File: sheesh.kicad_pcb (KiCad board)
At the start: 2 copper layers, 234.7 x 104.6 mm, 104 parts, among them J1 3305-0-15-80-47-27-10-0, J10 3305-0-15-80-47-27-10-0, J11 3305-0-15-80-47-27-10-0, J12 3305-0-15-80-47-27-10-0, J13 3305-0-15-80-47-27-10-0, J14 3305-0-15-80-47-27-10-0, J15 3305-0-15-80-47-27-10-0, J16 3305-0-15-80-47-27-10-0, J17 3305-0-15-80-47-27-10-0, J18 3305-0-15-80-47-27-10-0, J19 3305-0-15-80-47-27-10-0, J2 3305-0-15-80-47-27-10-0, J20 3305-0-15-80-47-27-10-0, J21 3305-0-15-80-47-27-10-0, J22 3305-0-15-80-47-27-10-0, J23 3305-0-15-80-47-27-10-0, J24 3305-0-15-80-47-27-10-0, J25 3305-0-15-80-47-27-10-0, J26 3305-0-15-80-47-27-10-0, J27 3305-0-15-80-47-27-10-0, J28 3305-0-15-80-47-27-10-0, J29 3305-0-15-80-47-27-10-0, J3 3305-0-15-80-47-27-10-0, J30 3305-0-15-80-47-27-10-0, J31 3305-0-15-80-47-27-10-0, J32 3305-0-15-80-47-27-10-0, J33 3305-0-15-80-47-27-10-0, J34 3305-0-15-80-47-27-10-0, J35 3305-0-15-80-47-27-10-0, J36 3305-0-15-80-47-27-10-0, J37 3305-0-15-80-47-27-10-0, J38 3305-0-15-80-47-27-10-0, J39 3305-0-15-80-47-27-10-0, J4 3305-0-15-80-47-27-10-0, J40 3305-0-15-80-47-27-10-0, J41 3305-0-15-80-47-27-10-0, J42 3305-0-15-80-47-27-10-0, J43 3305-0-15-80-47-27-10-0, J44 3305-0-15-80-47-27-10-0, J45 3305-0-15-80-47-27-10-0, J46 3305-0-15-80-47-27-10-0, J47 3305-0-15-80-47-27-10-0, J48 3305-0-15-80-47-27-10-0, J49 3305-0-15-80-47-27-10-0, J5 3305-0-15-80-47-27-10-0, J50 3305-0-15-80-47-27-10-0, J51 3305-0-15-80-47-27-10-0, J52 3305-0-15-80-47-27-10-0, J53 3305-0-15-80-47-27-10-0, J54 3305-0-15-80-47-27-10-0, J55 3305-0-15-80-47-27-10-0, J56 3305-0-15-80-47-27-10-0, J57 310-13-107-41-001000, J58 310-13-107-41-001000, J59 YZ00615050R-04, J6 3305-0-15-80-47-27-10-0, J60 YZ00615050R-04, J61 YZ00615050R-04, J62 YZ00615050R-04, J63 YZ00615050R-04, J64 310-13-107-41-001000, J65 310-13-107-41-001000, J66 YZ00615050R-04, J67 YZ00615050R-04, J68 YZ00615050R-04, J69 YZ00615050R-04, J7 3305-0-15-80-47-27-10-0, J70 YZ00615050R-04, J8 3305-0-15-80-47-27-10-0, J9 3305-0-15-80-47-27-10-0, SW1 SW_Push, SW10 SW_Push, SW11 SW_Push, SW12 SW_Push, SW13 SW_Push, SW14 SW_Push, SW15 SW_Push, SW16 SW_Push, SW17 SW_Push, SW18 SW_Push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

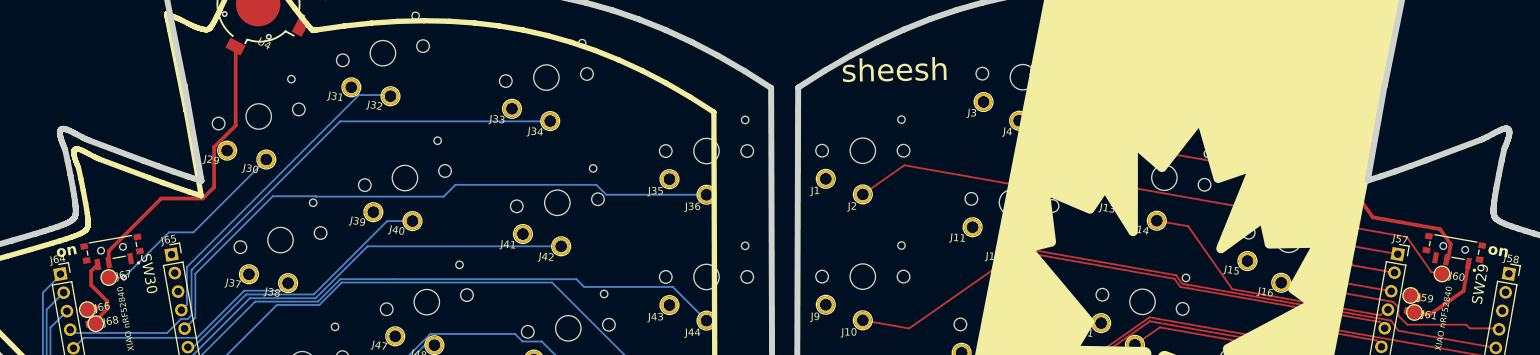
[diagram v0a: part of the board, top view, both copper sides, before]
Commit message: fix(sw-th_ssss811101): swap SW29 & SW30 symbol & footprint
Change PCM12SMTR to SSSS811101. The latter fits on the former's footprint, but the location was
slightly off fin  the cpl
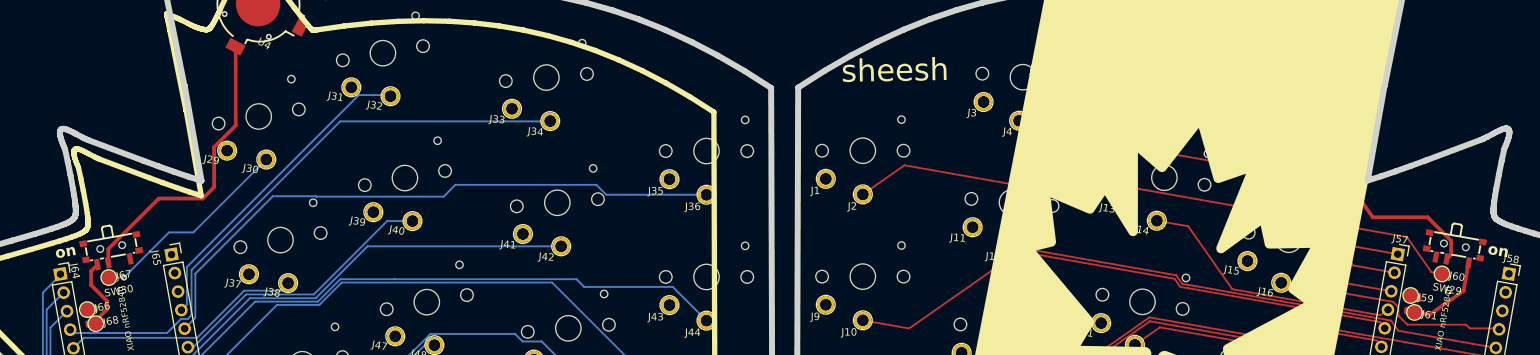
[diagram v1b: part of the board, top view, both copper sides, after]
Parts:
- SW29, SW30: footprint Sheesh:SW_PCM12SMTR -> Sheesh:SW-SMD_SSSS811101
- moved SW30 0.22 mm to (68.3, 90.8)
- moved SW29 0.10 mm to (249.6, 90.6)
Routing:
- net Net-(SW29-Pad2): track 39.7 -> 40.3 mm

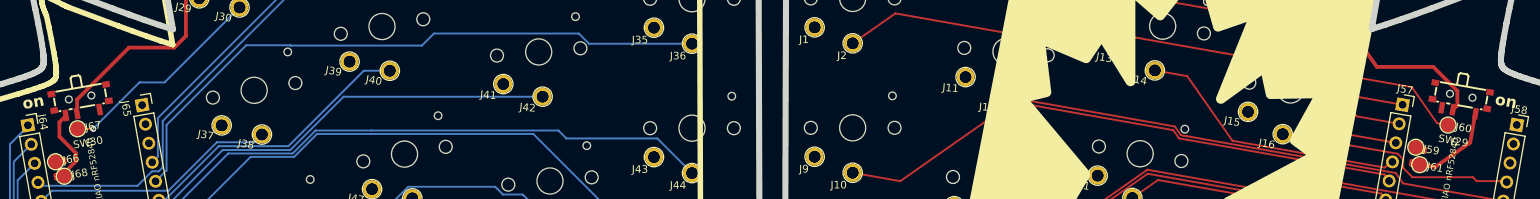
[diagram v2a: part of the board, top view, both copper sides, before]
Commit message: style(component): nudge switch away from pogo pin
nudge power switch for more comfortable clearance
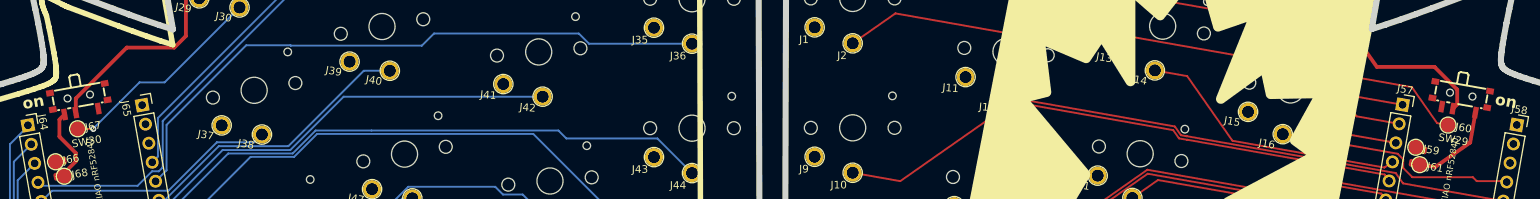
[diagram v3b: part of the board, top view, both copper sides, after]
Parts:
- moved SW30 0.22 mm to (68.2, 90.7)
- moved SW29 0.15 mm to (249.6, 90.4)
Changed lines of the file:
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@@
 		(fp_line
 			(start -8.63 -8.5)
-			(end 8.599913 -8.5)
+			(end 8.599912 -8.5)
 			(stroke
 				(width 0.12)
@@
 		(fp_arc
 			(start -8.994012 -8.099594)
-			(mid -8.898744 -8.378652)
+			(mid -8.898744 -8.378651)
 			(end -8.63 -8.5)
 			(stroke
@@
 		)
 		(fp_arc
-			(start 8.599913 -8.5)
-			(mid 8.878978 -8.404734)
+			(start 8.599912 -8.5)
+			(mid 8.878977 -8.404735)
 			(end 9.000321 -8.135989)
 			(stroke
@@
 		(fp_poly
 			(pts
-				(xy -1.1 -1.100002) (xy 1.100002 -1.1) (xy 1.1 1.100002) (xy -1.100002 1.1)
+				(xy -1.1 -1.100003) (xy 1.100003 -1.1) (xy 1.1 1.100003) (xy -1.100003 1.1)
 			)
 			(stroke
@@
 		(fp_line
 			(start -8.63 -8.5)
-			(end 8.599913 -8.5)
+			(end 8.599912 -8.5)
 			(stroke
 				(width 0.12)
@@
 		(fp_arc
 			(start -8.994012 -8.099594)
-			(mid -8.898744 -8.378652)
+			(mid -8.898744 -8.378651)
 			(end -8.63 -8.5)
 			(stroke
@@
 		)
 		(fp_arc
-			(start 8.599913 -8.5)
-			(mid 8.878978 -8.404734)
+			(start 8.599912 -8.5)
+			(mid 8.878977 -8.404735)
 			(end 9.000321 -8.135989)
 			(stroke
@@
 		(fp_poly
 			(pts
-				(xy -1.1 -1.100002) (xy 1.100002 -1.1) (xy 1.1 1.100002) (xy -1.100002 1.1)
+				(xy -1.1 -1.100003) (xy 1.100003 -1.1) (xy 1.1 1.100003) (xy -1.100003 1.1)
 			)
 			(stroke
@@
 		(fp_poly
 			(pts
-				(xy -1.1 -1.100002) (xy 1.100002 -1.1) (xy 1.1 1.100002) (xy -1.100002 1.1)
+				(xy -1.1 -1.100003) (xy 1.100003 -1.1) (xy 1.1 1.100003) (xy -1.100003 1.1)
 			)
 			(stroke
@@
 		(fp_line
 			(start -8.63 -8.5)
-			(end 8.599913 -8.5)
+			(end 8.599912 -8.5)
 			(stroke
 				(width 0.12)
@@
 		(fp_arc
 			(start -8.994012 -8.099594)
-			(mid -8.898744 -8.378652)
+			(mid -8.898744 -8.378651)
 			(end -8.63 -8.5)
 			(stroke
@@
 		)
 		(fp_arc
-			(start 8.599913 -8.5)
-			(mid 8.878978 -8.404734)
+			(start 8.599912 -8.5)
+			(mid 8.878977 -8.404735)
 			(end 9.000321 -8.135989)
 			(stroke
@@
 		(fp_line
 			(start -8.63 -8.5)
-			(end 8.599913 -8.5)
+			(end 8.599912 -8.5)
 			(stroke
 				(width 0.12)
@@
 		(fp_arc
 			(start -8.994012 -8.099594)
-			(mid -8.898744 -8.378652)
+			(mid -8.898744 -8.378651)
 			(end -8.63 -8.5)
 			(stroke
@@
 		)
 		(fp_arc
-			(start 8.599913 -8.5)
-			(mid 8.878978 -8.404734)
+			(start 8.599912 -8.5)
+			(mid 8.878977 -8.404735)
 			(end 9.000321 -8.135989)
 			(stroke
@@
 		(fp_line
 			(start -8.63 -8.5)
-			(end 8.599913 -8.5)
+			(end 8.599912 -8.5)
 			(stroke
 				(width 0.12)
@@
 		(fp_arc
 			(start -8.994012 -8.099594)
-			(mid -8.898744 -8.378652)
+			(mid -8.898744 -8.378651)
 			(end -8.63 -8.5)
 			(stroke
@@
 		)
 		(fp_arc
-			(start 8.599913 -8.5)
-			(mid 8.878978 -8.404734)
+			(start 8.599912 -8.5)
+			(mid 8.878977 -8.404735)
 			(end 9.000321 -8.135989)
 			(stroke
@@
 		(fp_poly
 			(pts
-				(xy -1.1 -1.100002) (xy 1.100002 -1.1) (xy 1.1 1.100002) (xy -1.100002 1.1)
+				(xy -1.1 -1.100003) (xy 1.100003 -1.1) (xy 1.1 1.100003) (xy -1.100003 1.1)
 			)
 			(stroke
@@
 		(fp_poly
 			(pts
-				(xy -1.100002 -1.1) (xy 1.1 -1.100002) (xy 1.100002 1.1) (xy -1.1 1.100002)
+				(xy -1.100003 -1.1) (xy 1.1 -1.100003) (xy 1.100003 1.1) (xy -1.1 1.100003)
 			)
 			(stroke
@@
 		(fp_poly
 			(pts
-				(xy -1.100002 -1.1) (xy 1.1 -1.100002) (xy 1.100002 1.1) (xy -1.1 1.100002)
+				(xy -1.100003 -1.1) (xy 1.1 -1.100003) (xy 1.100003 1.1) (xy -1.1 1.100003)
 			)
 			(stroke
@@
 		(fp_poly
 			(pts
-				(xy -1.100002 -1.1) (xy 1.1 -1.100002) (xy 1.100002 1.1) (xy -1.1 1.100002)
+				(xy -1.100003 -1.1) (xy 1.1 -1.100003) (xy 1.100003 1.1) (xy -1.1 1.100003)
 			)
 			(stroke
@@
 		(fp_line
 			(start -8.63 -8.5)
-			(end 8.599913 -8.5)
+			(end 8.599912 -8.5)
 			(stroke
 				(width 0.12)
@@
 		(fp_arc
 			(start -8.994012 -8.099594)
-			(mid -8.898744 -8.378652)
+			(mid -8.898744 -8.378651)
 			(end -8.63 -8.5)
 			(stroke
@@
 		)
 		(fp_arc
-			(start 8.599913 -8.5)
-			(mid 8.878978 -8.404734)
+			(start 8.599912 -8.5)
+			(mid 8.878977 -8.404735)
 			(end 9.000321 -8.135989)
 			(stroke
@@
 		(fp_poly
 			(pts
-				(xy -1.1 -1.100002) (xy 1.100002 -1.1) (xy 1.1 1.100002) (xy -1.100002 1.1)
+				(xy -1.1 -1.100003) (xy 1.100003 -1.1) (xy 1.1 1.100003) (xy -1.100003 1.1)
 			)
 			(stroke
@@
 		(fp_arc
 			(start 8.209767 0.991215)
-			(mid 6.834508 3.585383)
+			(mid 6.834507 3.585383)
 			(end 4.24 4.96)
 			(stroke
@@
 	(footprint "Sheesh:SW-SMD_SSSS811101"
 		(layer "F.Cu")
-		(at 68.326 90.805 -170)
+		(at 68.150142 90.676829 -170)
 		(property "Reference" "SW30"
 			(at 0 -5.55 -170)
@@
 		(fp_poly
 			(pts
-				(xy -1.100002 -1.1) (xy 1.1 -1.100002) (xy 1.100002 1.1) (xy -1.1 1.100002)
+				(xy -1.100003 -1.1) (xy 1.1 -1.100003) (xy 1.100003 1.1) (xy -1.1 1.100003)
 			)
 			(stroke
@@
 		(fp_poly
 			(pts
-				(xy -1.100002 -1.1) (xy 1.1 -1.100002) (xy 1.100002 1.1) (xy -1.1 1.100002)
+				(xy -1.100003 -1.1) (xy 1.1 -1.100003) (xy 1.100003 1.1) (xy -1.1 1.100003)
 			)
 			(stroke
@@
 	(footprint "Sheesh:SW-SMD_SSSS811101"
 		(layer "F.Cu")
-		(at 249.603859 90.575876 170)
+		(at 249.603859 90.424784 170)
 		(property "Reference" "SW29"
 			(at 0 -5.55 170)
@@
 	)
 	(segment
-		(start 67.66529 98.773295)
-		(end 67.66529 97.63729)
+		(start 67.66529 97.63729)
+		(end 65.532 95.504)
 		(width 0.5)
 		(layer "F.Cu")
@@
 	)
 	(segment
-		(start 67.66529 97.63729)
-		(end 65.532 95.504)
+		(start 65.784924 100.653661)
+		(end 67.66529 98.773295)
 		(width 0.5)
 		(layer "F.Cu")
@@
 	)
 	(segment
-		(start 65.532 93.6127)
-		(end 66.442079 92.702621)
+		(start 67.66529 98.773295)
+		(end 67.66529 97.63729)
 		(width 0.5)
 		(layer "F.Cu")
@@
 	)
 	(segment
-		(start 65.532 95.504)
-		(end 65.532 93.6127)
+		(start 65.532 93.265468)
+		(end 66.203479 92.593989)
 		(width 0.5)
 		(layer "F.Cu")
@@
 	)
 	(segment
-		(start 65.784924 100.653661)
-		(end 67.66529 98.773295)
+		(start 65.532 95.504)
+		(end 65.532 93.265468)
 		(width 0.5)
 		(layer "F.Cu")
@@
 	)
 	(segment
-		(start 238.593898 86.341105)
-		(end 246.017157 86.341105)
+		(start 233.308163 63.202874)
+		(end 235.123818 65.795898)
 		(width 0.5)
 		(layer "F.Cu")
@@
 	)
 	(segment
-		(start 232.927949 78.249292)
-		(end 238.593898 86.341105)
+		(start 238.593898 86.341105)
+		(end 246.168249 86.341105)
 		(width 0.5)
 		(layer "F.Cu")
@@
 	)
 	(segment
-		(start 249.174 89.497948)
-		(end 249.174 91.394191)
+		(start 232.927949 78.249292)
+		(end 238.593898 86.341105)
 		(width 0.5)
 		(layer "F.Cu")
@@
 	)
 	(segment
-		(start 233.308163 63.202874)
-		(end 235.123818 65.795898)
+		(start 246.168249 86.341105)
+		(end 249.154789 89.327645)
 		(width 0.5)
 		(layer "F.Cu")
@@
 	)
 	(segment
-		(start 249.174 91.394191)
-		(end 248.596099 91.972092)
+		(start 249.154789 89.327645)
+		(end 249.154789 91.26231)
 		(width 0.5)
 		(layer "F.Cu")
@@
 	)
 	(segment
-		(start 246.017157 86.341105)
-		(end 249.174 89.497948)
+		(start 249.154789 91.26231)
+		(end 248.596099 91.821)
 		(width 0.5)
 		(layer "F.Cu")
@@
 	)
 	(segment
-		(start 67.856549 90.626382)
-		(end 67.856549 92.461688)
+		(start 67.680691 90.498211)
+		(end 67.680691 92.333517)
 		(width 0.5)
 		(layer "F.Cu")
@@
 	)
 	(segment
-		(start 82.14329 76.859973)
-		(end 82.14329 82.28215)
+		(start 80.61929 83.80615)
+		(end 74.372752 83.80615)
 		(width 0.5)
 		(layer "F.Cu")
@@
 	)
 	(segment
-		(start 74.676781 83.80615)
-		(end 67.856549 90.626382)
+		(start 74.372752 83.80615)
+		(end 67.680691 90.498211)
 		(width 0.5)
 		(layer "F.Cu")
@@
 	)
 	(segment
-		(start 80.61929 83.80615)
-		(end 74.676781 83.80615)
+		(start 85.061817 63.248645)
+		(end 85.061817 73.941446)
 		(width 0.5)
 		(layer "F.Cu")
@@
 	)
 	(segment
-		(start 85.061817 63.248645)
-		(end 85.061817 73.941446)
+		(start 82.14329 76.859973)
+		(end 82.14329 82.28215)
 		(width 0.5)
 		(layer "F.Cu")

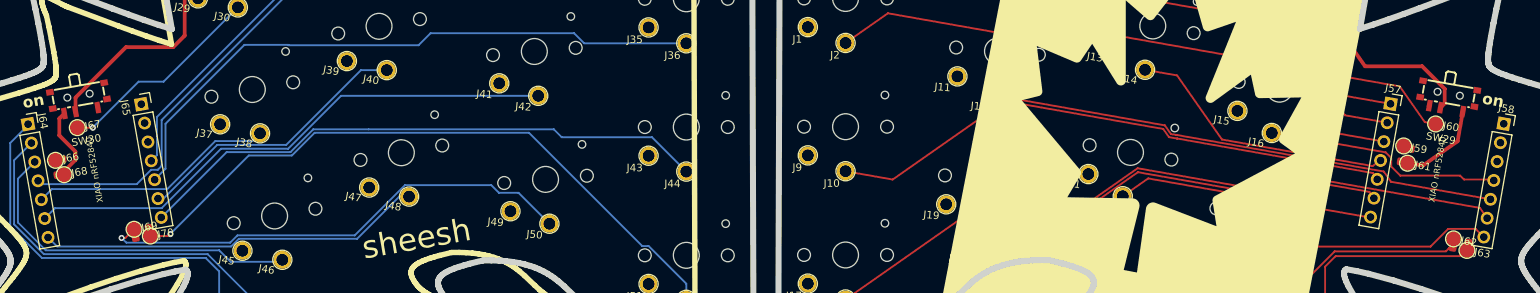
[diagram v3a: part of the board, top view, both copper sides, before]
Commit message: fix(pcb): add space between potential shorts
slightly adjust further recently updated switches and pogo pins to reduce the chance of failure
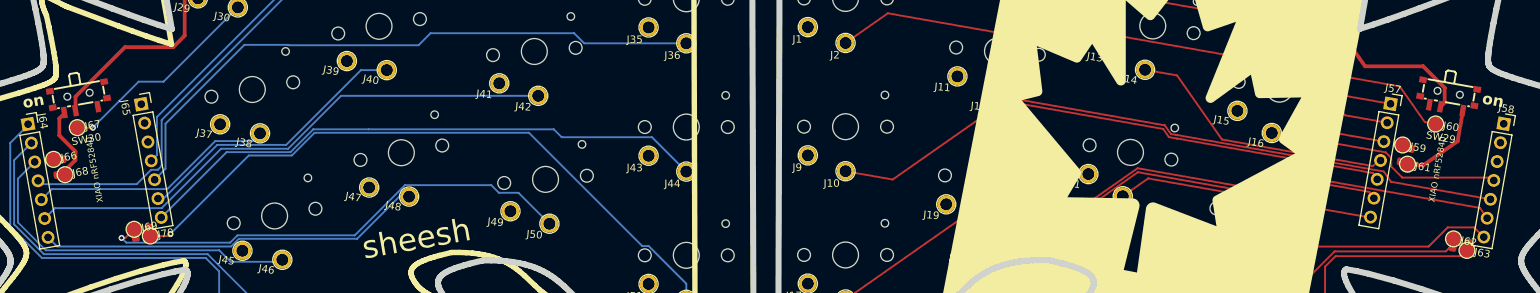
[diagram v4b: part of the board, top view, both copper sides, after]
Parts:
- moved J66 0.28 mm to (64.8, 98.7)
- moved J59 0.18 mm to (243.6, 96.8)
- moved SW29 0.13 mm to (249.6, 90.3)
- moved J61 0.13 mm to (244.2, 99.3)
- moved J68 0.13 mm to (66.3, 100.7)
- moved SW30 0.13 mm to (68.2, 90.6)
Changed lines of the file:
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@@
 		(fp_arc
 			(start -8.994012 -8.099594)
-			(mid -8.898744 -8.378651)
+			(mid -8.898743 -8.378651)
 			(end -8.63 -8.5)
 			(stroke
@@
 	(footprint "Sheesh:YZ00615050R-04"
 		(layer "F.Cu")
-		(at 65.024 98.806 10)
+		(at 64.77 98.679 10)
 		(descr "SMD Millmax Pogo Pin")
 		(tags "SMD Millmax Pogo Pin")
@@
 		(fp_arc
 			(start -8.994012 -8.099594)
-			(mid -8.898744 -8.378651)
+			(mid -8.898743 -8.378651)
 			(end -8.63 -8.5)
 			(stroke
@@
 	(footprint "Sheesh:YZ00615050R-04"
 		(layer "F.Cu")
-		(at 66.167 100.711 10)
+		(at 66.294 100.711 10)
 		(descr "SMD Millmax Pogo Pin")
 		(tags "SMD Millmax Pogo Pin")
@@
 		(fp_arc
 			(start -8.994012 -8.099594)
-			(mid -8.898744 -8.378651)
+			(mid -8.898743 -8.378651)
 			(end -8.63 -8.5)
 			(stroke
@@
 		(fp_arc
 			(start -8.994012 -8.099594)
-			(mid -8.898744 -8.378651)
+			(mid -8.898743 -8.378651)
 			(end -8.63 -8.5)
 			(stroke
@@
 		(fp_arc
 			(start -8.994012 -8.099594)
-			(mid -8.898744 -8.378651)
+			(mid -8.898743 -8.378651)
 			(end -8.63 -8.5)
 			(stroke
@@
 		(fp_arc
 			(start -8.994012 -8.099594)
-			(mid -8.898744 -8.378651)
+			(mid -8.898743 -8.378651)
 			(end -8.63 -8.5)
 			(stroke
@@
 	(footprint "Sheesh:SW-SMD_SSSS811101"
 		(layer "F.Cu")
-		(at 68.150142 90.676829 -170)
+		(at 68.150142 90.551 -170)
 		(property "Reference" "SW30"
 			(at 0 -5.55 -170)
@@
 	(footprint "Sheesh:YZ00615050R-04"
 		(layer "F.Cu")
-		(at 244.221 99.187 -10)
+		(at 244.221 99.314 -10)
 		(descr "SMD Millmax Pogo Pin")
 		(tags "SMD Millmax Pogo Pin")
@@
 	(footprint "Sheesh:YZ00615050R-04"
 		(layer "F.Cu")
-		(at 243.713 96.901 -10)
+		(at 243.586 96.774 -10)
 		(descr "SMD Millmax Pogo Pin")
 		(tags "SMD Millmax Pogo Pin")
@@
 	(footprint "Sheesh:SW-SMD_SSSS811101"
 		(layer "F.Cu")
-		(at 249.603859 90.424784 170)
+		(at 249.603859 90.297 170)
 		(property "Reference" "SW29"
 			(at 0 -5.55 170)
@@
 	)
 	(segment
-		(start 251.714 101.346)
-		(end 251.206 100.838)
+		(start 242.062 99.631289)
+		(end 242.062 98.483304)
 		(width 0.25)
 		(layer "F.Cu")
@@
 	)
 	(segment
-		(start 241.331556 97.75286)
-		(end 226.341116 95.109641)
-		(width 0.25)
-		(layer "F.Cu")
-		(net 10)
-	)
-	(segment
-		(start 255.656684 101.471892)
-		(end 255.530792 101.346)
-		(width 0.25)
-		(layer "F.Cu")
-		(net 10)
-	)
-	(segment
-		(start 243.268711 100.838)
-		(end 242.062 99.631289)
+		(start 242.062 98.483304)
+		(end 241.331556 97.75286)
 		(width 0.25)
 		(layer "F.Cu")
@@
 	)
 	(segment
-		(start 242.062 99.631289)
-		(end 242.062 98.483304)
+		(start 255.276792 101.092)
+		(end 243.522711 101.092)
 		(width 0.25)
 		(layer "F.Cu")
@@
 	)
 	(segment
-		(start 251.206 100.838)
-		(end 243.268711 100.838)
+		(start 241.331556 97.75286)
+		(end 226.341116 95.109641)
 		(width 0.25)
 		(layer "F.Cu")
@@
 	)
 	(segment
-		(start 242.062 98.483304)
-		(end 241.331556 97.75286)
+		(start 255.656684 101.471892)
+		(end 255.276792 101.092)
 		(width 0.25)
 		(layer "F.Cu")
@@
 	)
 	(segment
-		(start 255.530792 101.346)
-		(end 251.714 101.346)
+		(start 243.522711 101.092)
+		(end 242.062 99.631289)
 		(width 0.25)
 		(layer "F.Cu")
@@
 	)
 	(segment
-		(start 249.61 107.895)
-		(end 253.252358 107.895)
+		(start 249.555 107.696)
+		(end 253.053358 107.696)
 		(width 0.25)
 		(layer "F.Cu")
@@
 	)
 	(segment
-		(start 224.987464 110.236)
-		(end 247.269 110.236)
+		(start 247.015 110.236)
+		(end 249.555 107.696)
 		(width 0.25)
 		(layer "F.Cu")
@@
 	)
 	(segment
-		(start 223.280547 111.942917)
-		(end 224.987464 110.236)
+		(start 224.987464 110.236)
+		(end 247.015 110.236)
 		(width 0.25)
 		(layer "F.Cu")
@@
 	)
 	(segment
-		(start 253.252358 107.895)
+		(start 253.053358 107.696)
 		(end 254.333485 108.976127)
 		(width 0.25)
@@
 	)
 	(segment
-		(start 247.269 110.236)
-		(end 249.61 107.895)
+		(start 223.280547 111.942917)
+		(end 224.987464 110.236)
 		(width 0.25)
 		(layer "F.Cu")
@@
 	)
 	(segment
-		(start 233.308163 63.202874)
-		(end 235.123818 65.795898)
+		(start 235.123818 65.795898)
+		(end 232.927949 78.249292)
 		(width 0.5)
 		(layer "F.Cu")
@@
 	)
 	(segment
-		(start 238.593898 86.341105)
-		(end 246.168249 86.341105)
+		(start 233.308163 63.202874)
+		(end 235.123818 65.795898)
 		(width 0.5)
 		(layer "F.Cu")
@@
 	)
 	(segment
-		(start 232.927949 78.249292)
-		(end 238.593898 86.341105)
+		(start 249.154789 89.199861)
+		(end 249.154789 91.134526)
 		(width 0.5)
 		(layer "F.Cu")
@@
 	)
 	(segment
-		(start 246.168249 86.341105)
-		(end 249.154789 89.327645)
+		(start 246.296033 86.341105)
+		(end 249.154789 89.199861)
 		(width 0.5)
 		(layer "F.Cu")
@@
 	)
 	(segment
-		(start 249.154789 89.327645)
-		(end 249.154789 91.26231)
+		(start 238.593898 86.341105)
+		(end 246.296033 86.341105)
 		(width 0.5)
 		(layer "F.Cu")
@@
 	)
 	(segment
-		(start 235.123818 65.795898)
-		(end 232.927949 78.249292)
+		(start 232.927949 78.249292)
+		(end 238.593898 86.341105)
 		(width 0.5)
 		(layer "F.Cu")
@@
 	)
 	(segment
-		(start 249.154789 91.26231)
-		(end 248.596099 91.821)
+		(start 249.154789 91.134526)
+		(end 248.596099 91.693216)
 		(width 0.5)
 		(layer "F.Cu")
@@
 	)
 	(segment
-		(start 67.680691 90.498211)
-		(end 67.680691 92.333517)
+		(start 74.246923 83.80615)
+		(end 67.680691 90.372382)
 		(width 0.5)
 		(layer "F.Cu")
@@
 	)
 	(segment
-		(start 80.61929 83.80615)
-		(end 74.372752 83.80615)
+		(start 82.14329 76.859973)
+		(end 82.14329 82.28215)
 		(width 0.5)
 		(layer "F.Cu")
@@
 	)
 	(segment
-		(start 82.14329 82.28215)
-		(end 80.61929 83.80615)
+		(start 80.61929 83.80615)
+		(end 74.246923 83.80615)
 		(width 0.5)
 		(layer "F.Cu")
@@
 	)
 	(segment
-		(start 74.372752 83.80615)
-		(end 67.680691 90.498211)
+		(start 85.061817 73.941446)
+		(end 82.14329 76.859973)
 		(width 0.5)
 		(layer "F.Cu")
@@
 	)
 	(segment
-		(start 85.061817 73.941446)
-		(end 82.14329 76.859973)
+		(start 67.680691 90.372382)
+		(end 67.680691 92.207688)
 		(width 0.5)
 		(layer "F.Cu")
@@
 	)
 	(segment
-		(start 85.061817 63.248645)
-		(end 85.061817 73.941446)
+		(start 82.14329 82.28215)
+		(end 80.61929 83.80615)
 		(width 0.5)
 		(layer "F.Cu")
@@
 	)
 	(segment
-		(start 82.14329 76.859973)
-		(end 82.14329 82.28215)
+		(start 85.061817 63.248645)
+		(end 85.061817 73.941446)
 		(width 0.5)
 		(layer "F.Cu")
